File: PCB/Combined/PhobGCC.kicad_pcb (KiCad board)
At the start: 2 copper layers, 143 x 91.4 mm, 75 parts, among them J1 Conn_01x06_Female, J2 Conn_01x04_Female, J3 Conn_01x01_Male, J4 Conn_01x04_Male, J5 Conn_01x02_Male, Q1 Q_NMOS_GSD, Q2 Q_PMOS_GDS, Q3 Q_NMOS_GSD, SW1 A, SW10 Dup, SW11 Dright, SW12 Ddown, SW2 B, SW3 X, SW4 Y, SW5 Start, SW6 L, SW7 R, SW8 1825027-5, SW9 Dleft, U1 Teensy4.0, U2 2x DRV5053CAQLPGM Hall Effect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, U3 GP2S60-MFG, U4 GP2S60-MFG, U5 Stickbox_Assembly

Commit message: update silkscreen
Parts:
- added G***: LOGO, Gamecube MB:Ghost Logo, F.Cu at (55.4, 73.5)
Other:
- board text added: "20220525"
- board text removed: "20220510"

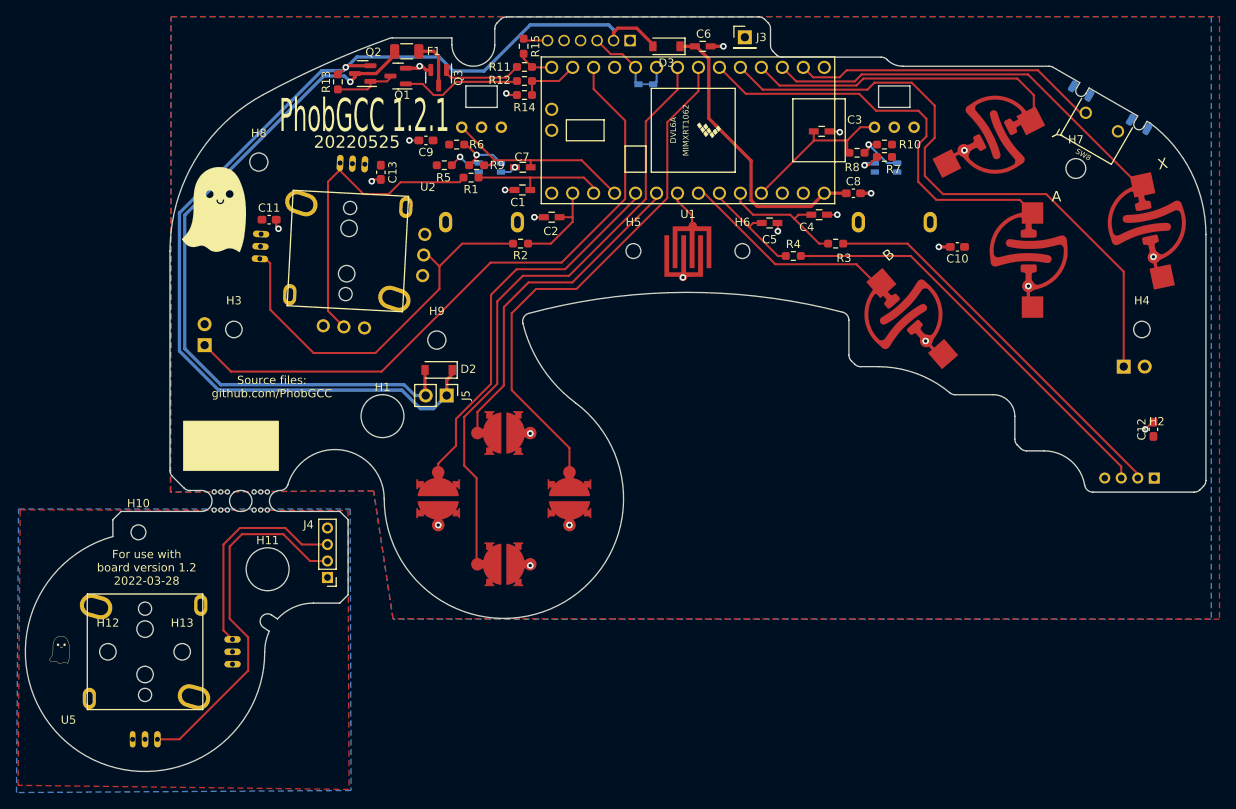
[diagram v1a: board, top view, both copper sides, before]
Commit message: Made all designators for sitches visible and moved a couple. Made the ghosts smile a bit thicker.
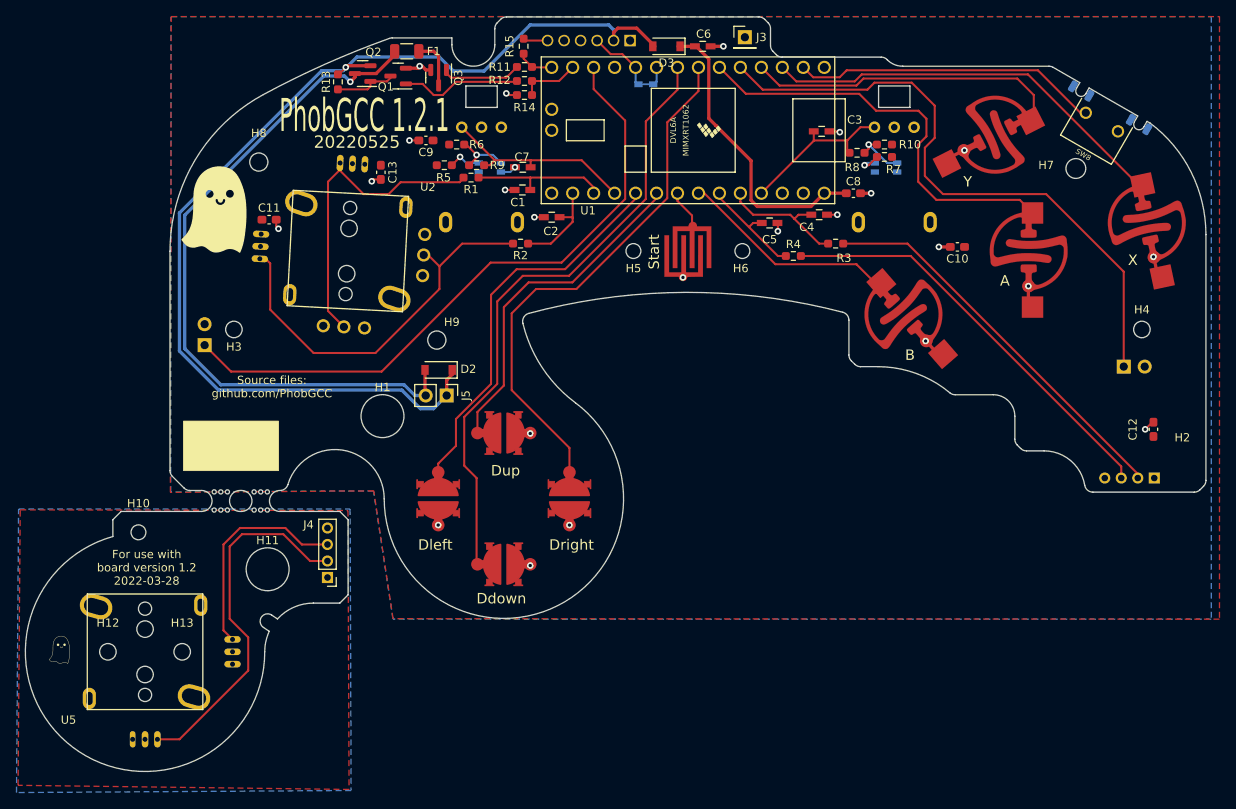
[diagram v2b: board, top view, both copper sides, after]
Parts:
- G***: footprint Gamecube MB:Ghost Logo -> PhobGCC_Footprints:Ghost Logo 2

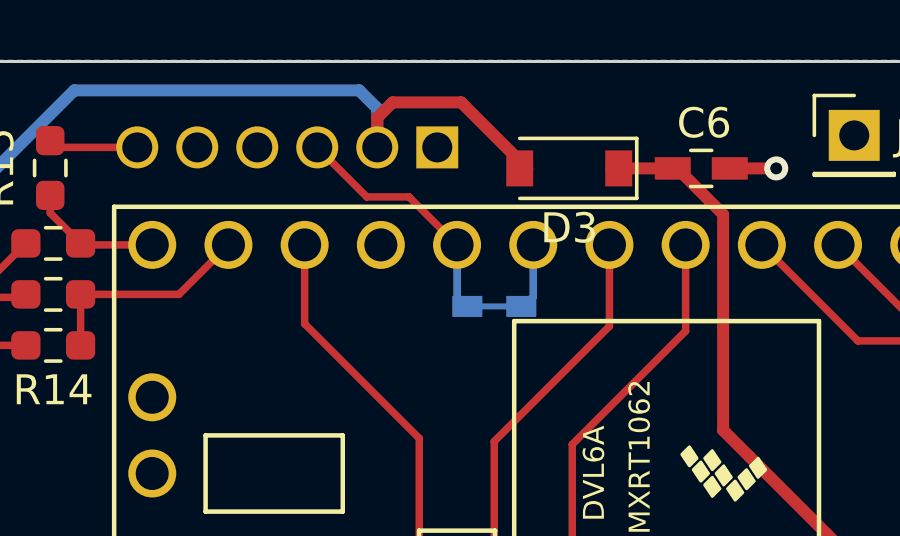
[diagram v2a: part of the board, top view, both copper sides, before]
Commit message: Rerouted the data signal to pin 7 of the teensy first, then to pin 8. This will allow the trace between pins 7 and 8 to be cut and a diode installed if the half-duplex communication needs to be reverted for some reason.
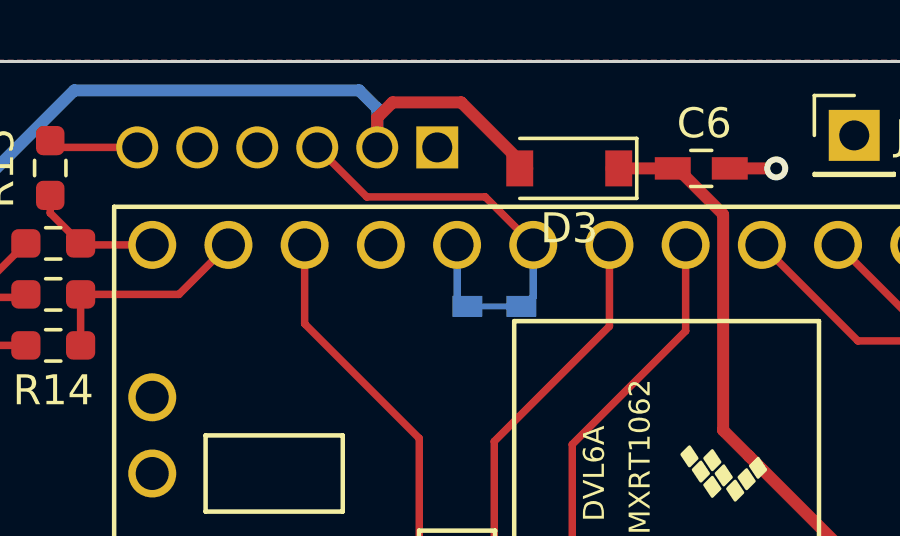
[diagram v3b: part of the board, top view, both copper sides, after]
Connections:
- D1 pad 1: /Data -> Net-(D1-Pad1)
- D1 pad 2: Net-(D1-Pad2) -> /Data
- U1 pad 10: /Data -> Net-(D1-Pad1)
- U1 pad 9: Net-(D1-Pad2) -> /Data
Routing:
- net /Data: track 8.17 -> 10.7 mm
- net Net-(D1-Pad2): track 2.18 -> 0.00 mm
- net Net-(D1-Pad1): track 0.00 -> 2.16 mm
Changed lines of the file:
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@@
   (net 40 "/Data")
   (net 41 "unconnected-(U1-Pad11)")
-  (net 42 "Net-(D1-Pad2)")
+  (net 42 "Net-(D1-Pad1)")
   (net 43 "VCC")
   (net 44 "Net-(J4-Pad2)")
@@
       (net 15 "/Ddown") (pinfunction "6_OUT1D") (pintype "bidirectional"))
     (pad "9" thru_hole circle (at 3.81 7.62 180) (size 1.6 1.6) (drill 1.1) (layers *.Cu *.Mask)
-      (net 42 "Net-(D1-Pad2)") (pinfunction "7_RX2_OUT1A") (pintype "bidirectional"))
+      (net 40 "/Data") (pinfunction "7_RX2_OUT1A") (pintype "bidirectional"))
     (pad "10" thru_hole circle (at 6.35 7.62 180) (size 1.6 1.6) (drill 1.1) (layers *.Cu *.Mask)
-      (net 40 "/Data") (pinfunction "8_TX2_IN1") (pintype "bidirectional"))
+      (net 42 "Net-(D1-Pad1)") (pinfunction "8_TX2_IN1") (pintype "bidirectional"))
     (pad "11" thru_hole circle (at 8.89 7.62 180) (size 1.6 1.6) (drill 1.1) (layers *.Cu *.Mask)
       (net 41 "unconnected-(U1-Pad11)") (pinfunction "9_OUT1C") (pintype "bidirectional"))
@@
     (fp_line (start 0.1 0.2) (end -0.2 0) (layer "B.Fab") (width 0.1))
     (pad "1" smd rect (at -0.9 0 180) (size 1 0.7) (layers "B.Cu" "B.Paste" "B.Mask")
-      (net 40 "/Data") (pinfunction "K") (pintype "passive"))
+      (net 42 "Net-(D1-Pad1)") (pinfunction "K") (pintype "passive"))
     (pad "2" smd rect (at 0.9 0 180) (size 1 0.7) (layers "B.Cu" "B.Paste" "B.Mask")
-      (net 42 "Net-(D1-Pad2)") (pinfunction "A") (pintype "passive"))
+      (net 40 "/Data") (pinfunction "A") (pintype "passive"))
     (model "${KISYS3DMOD}/Diode_SMD.3dshapes/D_SOD-523.wrl"
       (offset (xyz 0 0 0))
@@
   (segment (start 51.64952 90.23096) (end 56.01856 94.6) (width 0.4) (layer "B.Cu") (net 39))
   (segment (start 56.01856 94.6) (end 78.21856 94.6) (width 0.4) (layer "B.Cu") (net 39))
+  (segment (start 107.2 54.55) (end 108.8 56.15) (width 0.25) (layer "F.Cu") (net 40))
   (segment (start 101.6 52.9) (end 103.25 54.55) (width 0.25) (layer "F.Cu") (net 40))
-  (segment (start 104.66 54.55) (end 106.26 56.15) (width 0.25) (layer "F.Cu") (net 40))
-  (segment (start 103.25 54.55) (end 104.66 54.55) (width 0.25) (layer "F.Cu") (net 40))
-  (segment (start 106.26 56.15) (end 106.26 57.93452) (width 0.25) (layer "B.Cu") (net 40))
-  (segment (start 106.26 57.93452) (end 106.52548 58.2) (width 0.25) (layer "B.Cu") (net 40))
-  (segment (start 108.8 57.87452) (end 108.47452 58.2) (width 0.25) (layer "B.Cu") (net 42))
-  (segment (start 108.8 56.15) (end 108.8 57.87452) (width 0.25) (layer "B.Cu") (net 42))
+  (segment (start 103.25 54.55) (end 107.2 54.55) (width 0.25) (layer "F.Cu") (net 40))
+  (segment (start 108.8 57.87452) (end 108.47452 58.2) (width 0.25) (layer "B.Cu") (net 40))
+  (segment (start 108.8 56.15) (end 108.8 57.87452) (width 0.25) (layer "B.Cu") (net 40))
+  (segment (start 106.26 56.15) (end 106.26 57.93452) (width 0.25) (layer "B.Cu") (net 42))
+  (segment (start 106.26 57.93452) (end 106.52548 58.2) (width 0.25) (layer "B.Cu") (net 42))
   (segment (start 57.084 122.951) (end 59.334 125.201) (width 0.25) (layer "F.Cu") (net 44))
   (segment (start 68.934 115.951) (end 66.834 115.951) (width 0.25) (layer "F.Cu") (net 44))

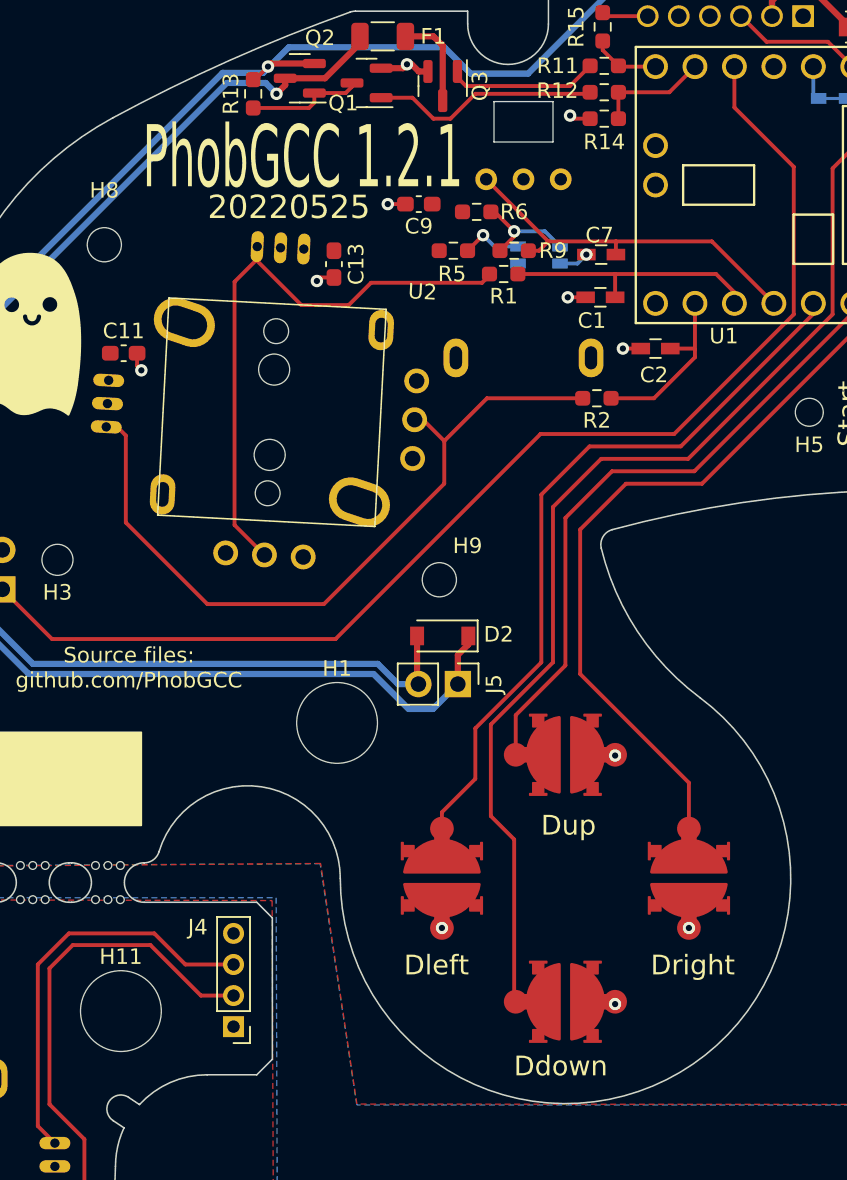
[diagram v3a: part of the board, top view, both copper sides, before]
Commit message: fix dpad footprints
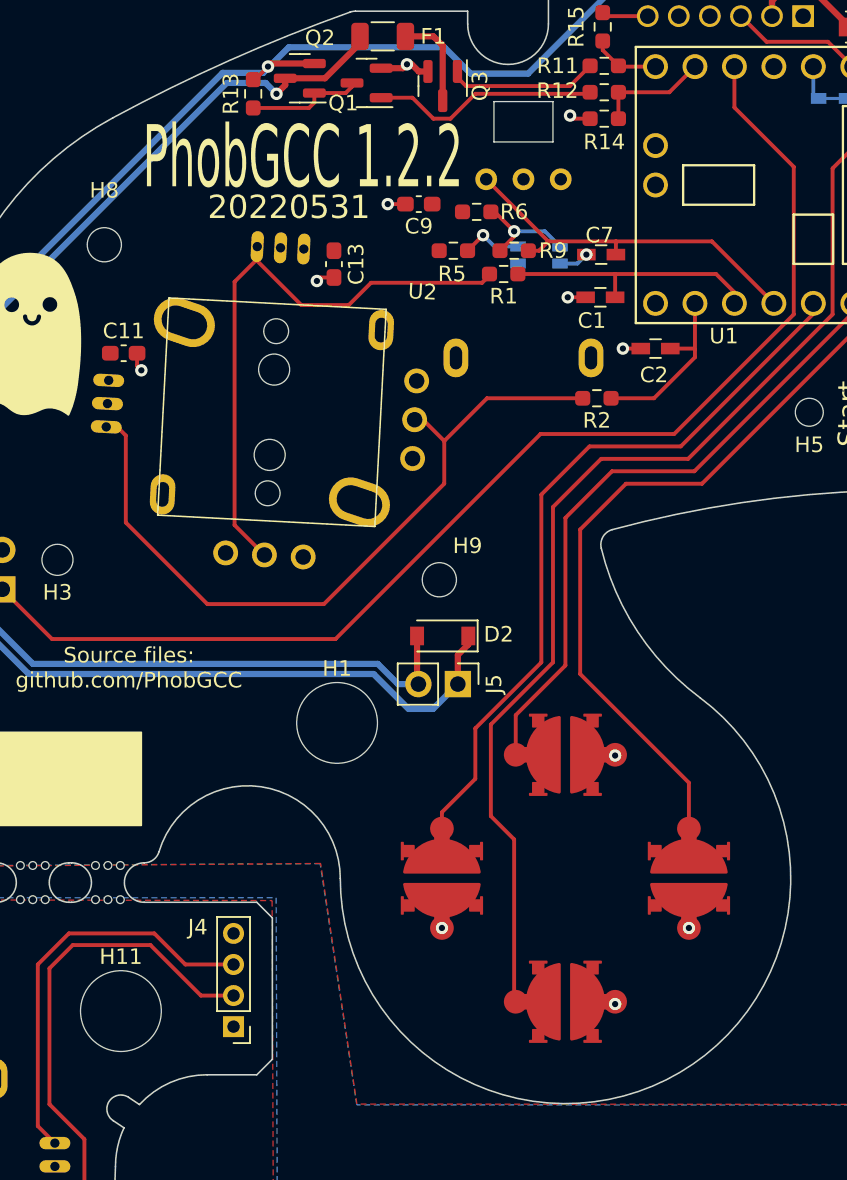
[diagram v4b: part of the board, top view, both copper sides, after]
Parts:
- SW10, SW11, SW12, SW9: footprint PhobGCC_Footprints:Dpad_Contact_TL3315NF_2 -> PhobGCC_Footprints:Dpad_Contact_TL3315NF_3
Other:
- board text added: "20220531"
- board text added: "PhobGCC 1.2.2"
- board text removed: "20220525"
- board text removed: "PhobGCC 1.2.1"
